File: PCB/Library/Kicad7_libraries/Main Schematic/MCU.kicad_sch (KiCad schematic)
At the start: 27 parts, among them J1 Conn_ARM_JTAG_SWD_10, SW1 SW_Push, U1 STM32F051C6Tx, U2 CP2102N-Axx-xQFN20

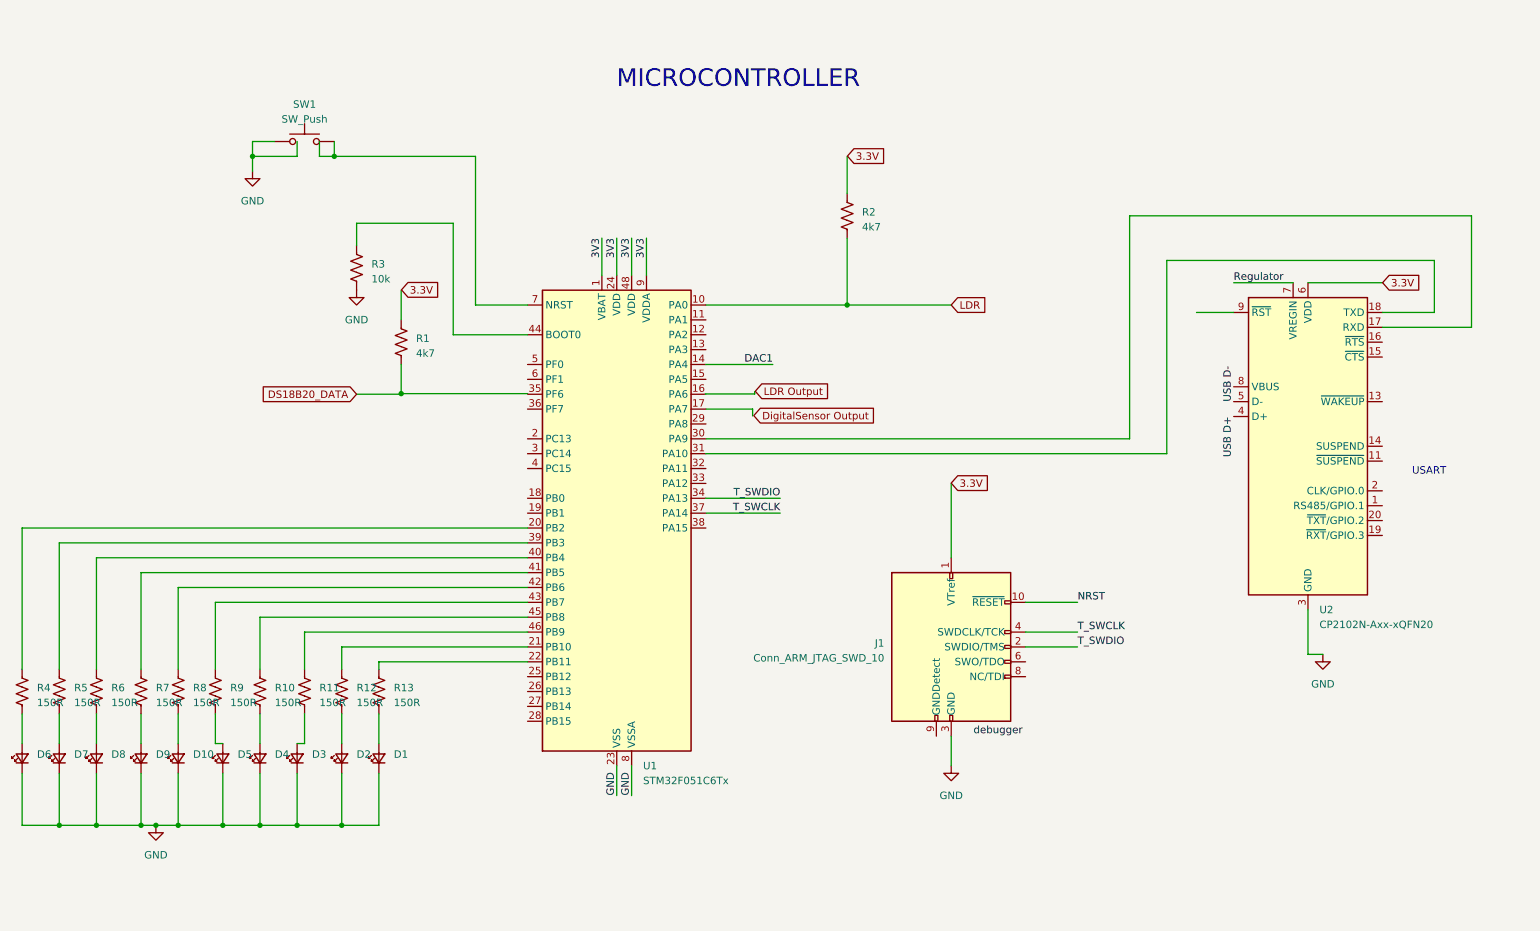
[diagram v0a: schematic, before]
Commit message: I recreated our schematics into hierachy sheets instead of individual sheets
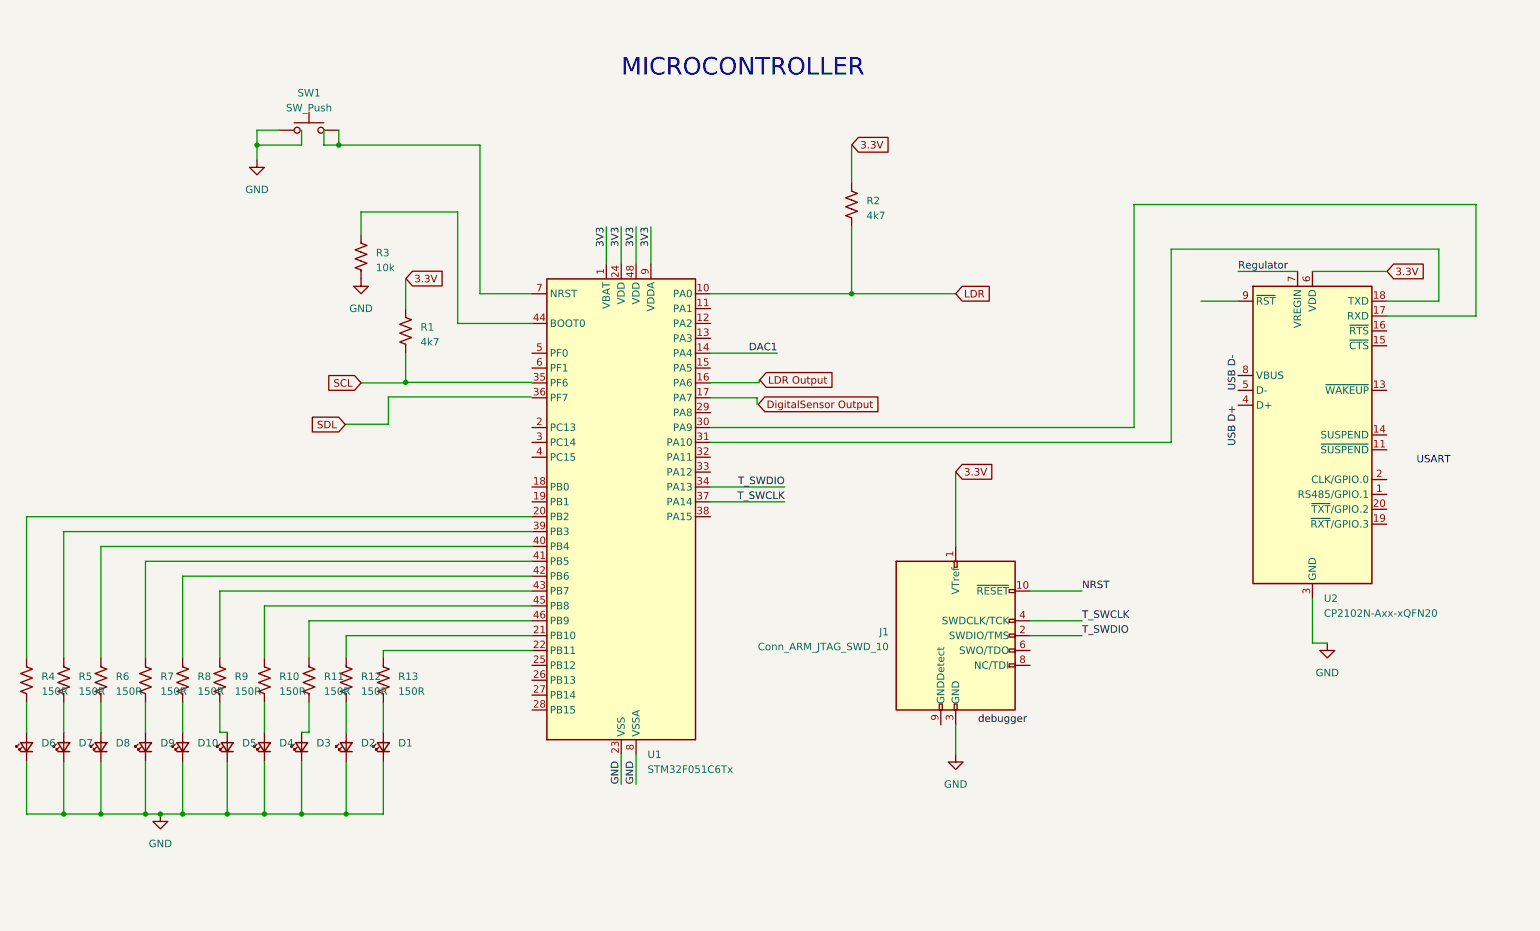
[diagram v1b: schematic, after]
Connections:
- net DS18B20_DATA renamed SCL

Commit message: Updated the MCU circuit
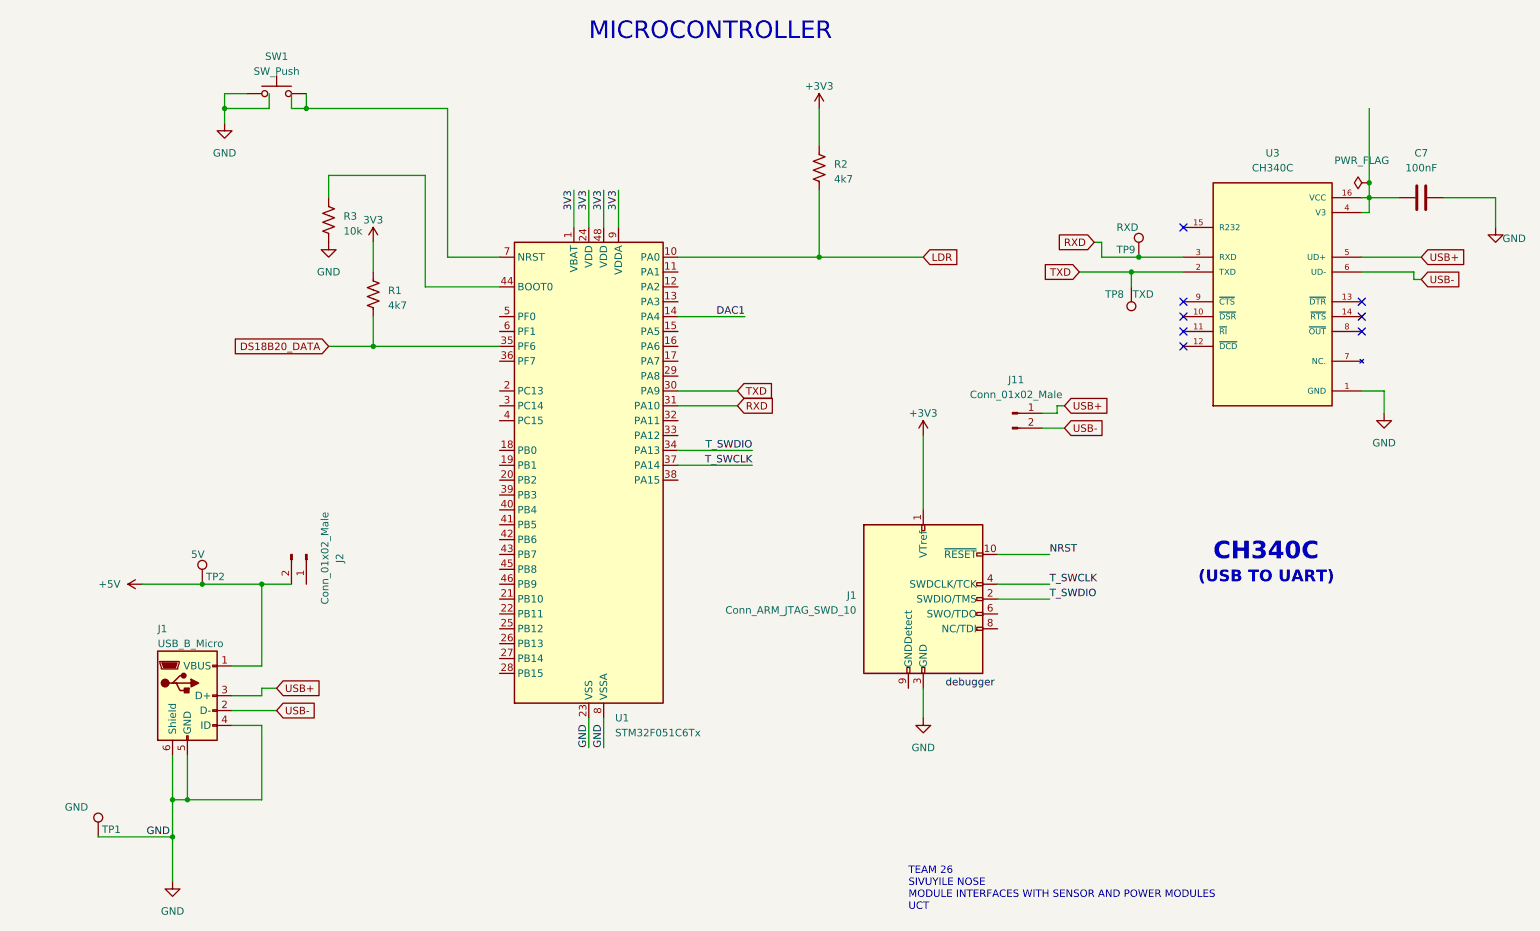
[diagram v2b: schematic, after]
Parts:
- removed D1, D10, D2, D3, D4, D5, D6, D7, D8, D9: LED_Small, symbol Device:LED_Small
- removed R10, R11, R12, R13, R4, R5, R6, R7, R8, R9: 150R, symbol Device:R_US
- removed U2: CP2102N-Axx-xQFN20, Package_DFN_QFN:SiliconLabs_QFN-20-1EP_3x3mm_P0.5mm, symbol Interface_USB:CP2102N-Axx-xQFN20
- added C7: 100nF, 100NF_C:CAPC1005X55N, symbol Device:C
- added J1: USB_B_Micro, Connector_USB:USB_Micro-B_GCT_USB3076-30-A, symbol Connector:USB_B_Micro
- added J11, J2: Conn_01x02_Male, Connector_PinHeader_2.54mm:PinHeader_1x02_P2.54mm_Vertical, symbol Connector:Conn_01x02_Male
- added TP1: GND, TestPoint:TestPoint_Pad_1.0x1.0mm, symbol Connector:TestPoint
- added TP2: 5V, TestPoint:TestPoint_Pad_1.0x1.0mm, symbol Connector:TestPoint
- added TP8: TXD, TestPoint:TestPoint_Pad_1.0x1.0mm, symbol Connector:TestPoint
- added TP9: RXD, TestPoint:TestPoint_Pad_1.0x1.0mm, symbol Connector:TestPoint
- added U3: CH340C, CH340:SOIC127P600X180-16N, symbol CH340C:CH340C
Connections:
- net SCL is gone; now on net DS18B20_DATA: R1.2
- net GND: now also C7.2, J1.4 (ID), J1.5 (GND), J1.6 (Shield), TP1.1, U3.1 (GND)
- net +3V3: now reaches R2.1
- net +3V3: now also J1.1 (VTref), R1.1
- net TXD: now reaches U1.30 (PA9)
- net TXD: now also TP8.1, U3.2 (TXD)
- net RXD: now reaches U1.31 (PA10)
- net RXD: now also TP9.1, U3.3 (RXD)
- net DS18B20_DATA: now reaches U1.35 (PF6)
- new net: C7.1, U3.16 (VCC), U3.4 (V3)
- new net +5V: J1.1 (VBUS), J2.2 (Pin_2), TP2.1
- new net USB+: J1.3 (D+), J11.1 (Pin_1), U3.5 (UD+)
- new net USB-: J1.2 (D-), J11.2 (Pin_2), U3.6 (UD-)
- no-connect marks 0 -> 8
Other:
- note added: "(USB TO UART)"
- note added: "CH340C"
- note added: "TEAM 26 SIVUYILE NOSE MODULE INTERFACES WITH SENSOR AND POWER MODULES UCT"
- note removed: "USART"

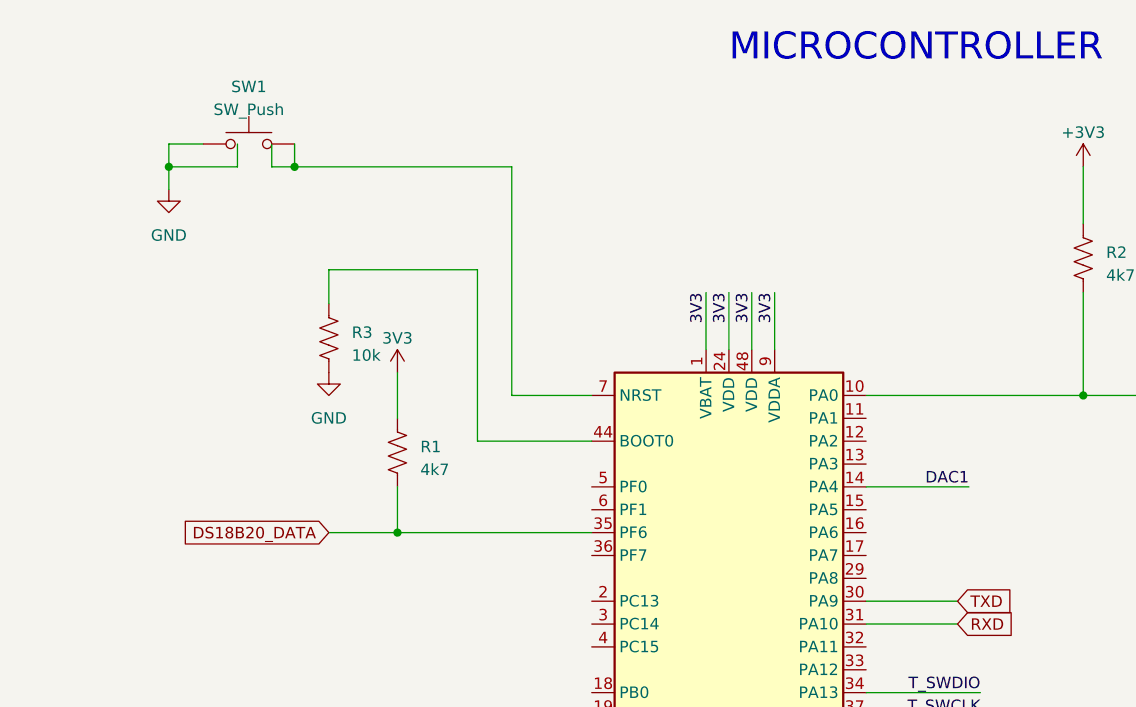
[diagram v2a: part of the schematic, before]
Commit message: Updated the MCU
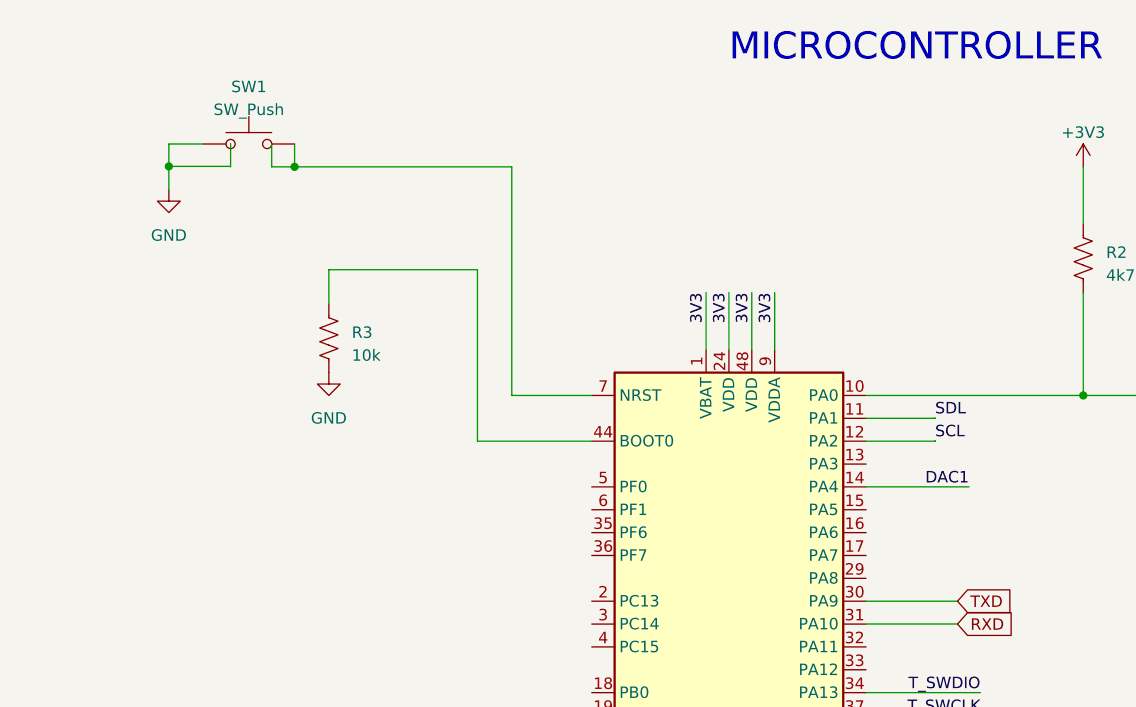
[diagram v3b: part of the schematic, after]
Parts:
- removed R1: 4k7, symbol Device:R_US
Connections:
- net SDL: now reaches U1.11 (PA1)
- net SCL: now reaches U1.12 (PA2)
- net DS18B20_DATA: no longer names the net of U1.35 (PF6)

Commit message: updated sche
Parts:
- removed J1: USB_B_Micro, Connector_USB:USB_Micro-B_GCT_USB3076-30-A, symbol Connector:USB_B_Micro
- removed J2: Conn_01x02_Male, Connector_PinHeader_2.54mm:PinHeader_1x02_P2.54mm_Vertical, symbol Connector:Conn_01x02_Male
- removed TP1: GND, TestPoint:TestPoint_Pad_1.0x1.0mm, symbol Connector:TestPoint
- removed TP2: 5V, TestPoint:TestPoint_Pad_1.0x1.0mm, symbol Connector:TestPoint
